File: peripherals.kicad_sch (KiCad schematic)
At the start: 61 parts, among them J8 Conn_02x25_Odd_Even, U1 MX6UL-VM

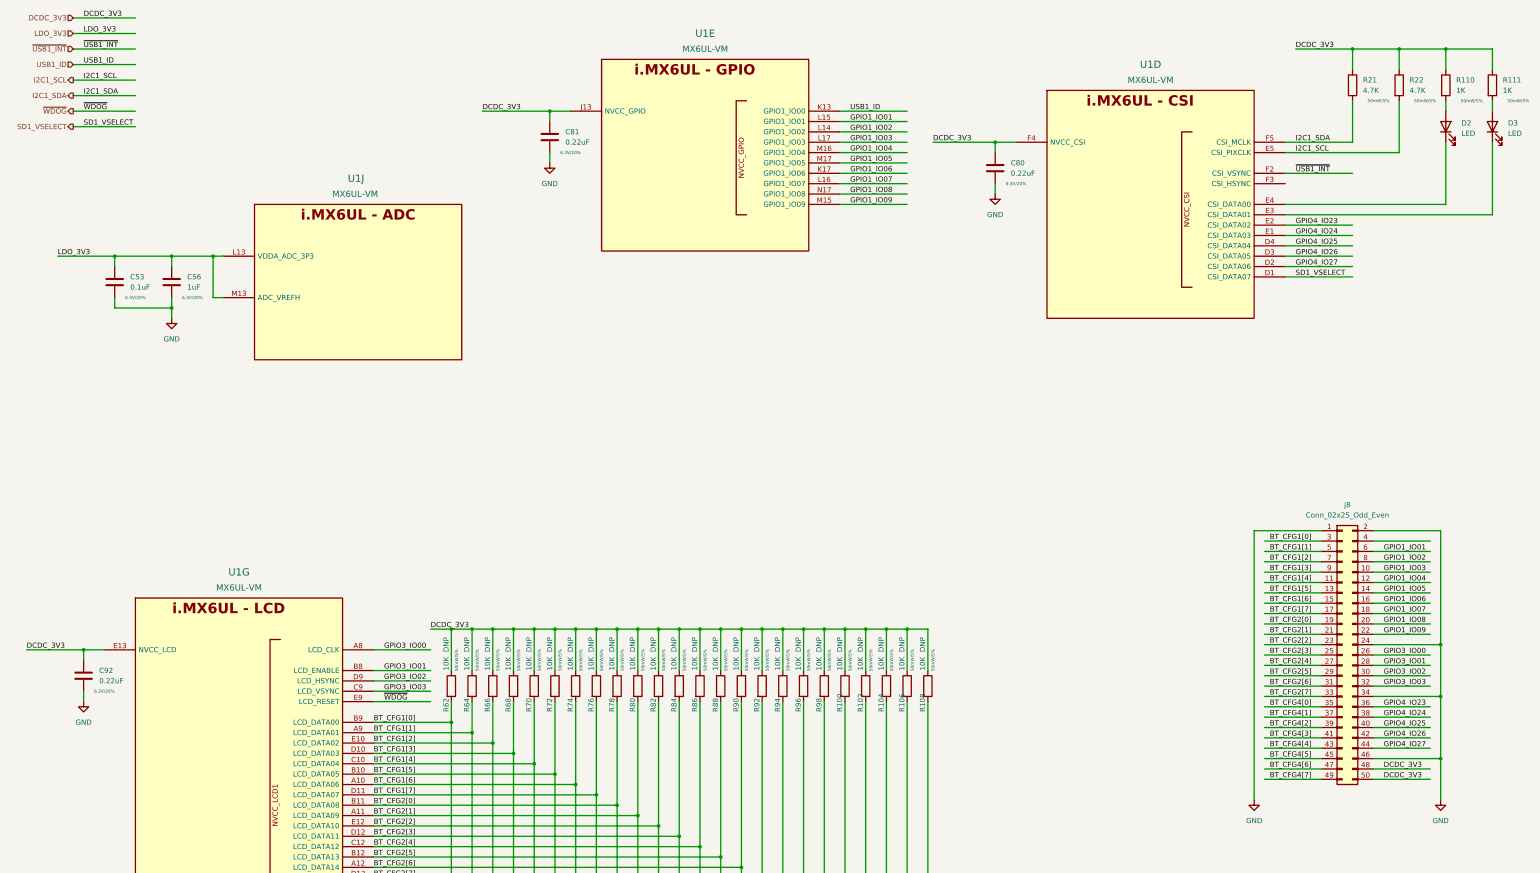
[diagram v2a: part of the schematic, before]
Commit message: most of sch done, inital component pcb placement
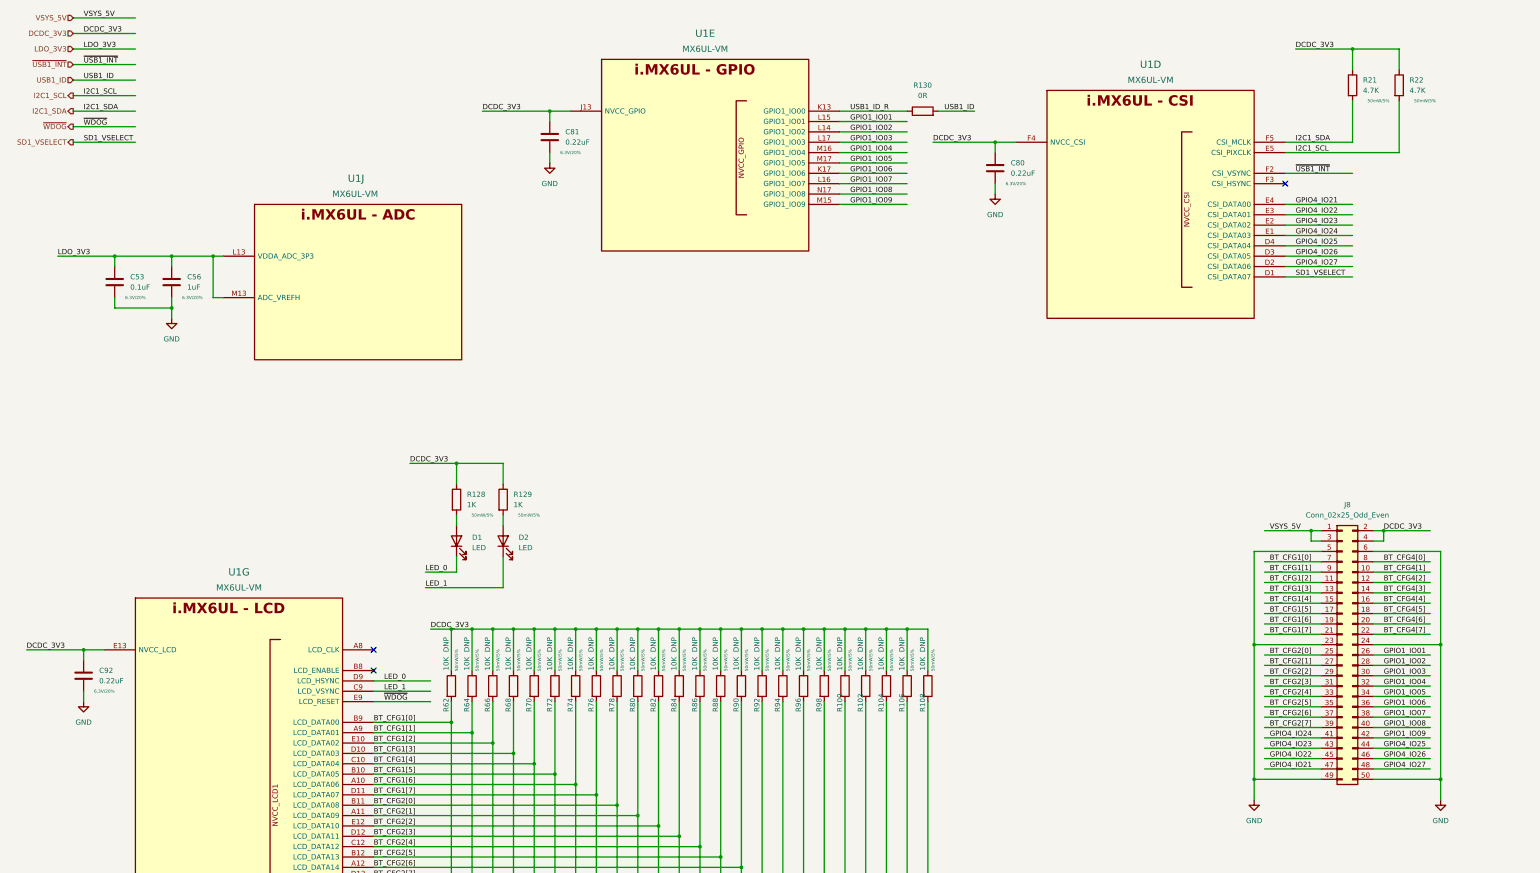
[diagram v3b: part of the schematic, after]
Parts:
- removed D3: LED, LED_SMD:LED_0603_1608Metric, symbol Device:LED
- removed R110, R111: 1K, Resistor_SMD:R_0402_1005Metric, symbol Device:R
- added D1: LED, LED_SMD:LED_0603_1608Metric, symbol Device:LED
- added R128, R129: 1K, Resistor_SMD:R_0402_1005Metric, symbol Device:R
- added R130: 0R, Resistor_SMD:R_0402_1005Metric, symbol Device:R
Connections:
- net BT_CFG1[0]: now also J8.7 (Pin_7); no longer J8.3 (Pin_3)
- net BT_CFG1[1]: now also J8.9 (Pin_9); no longer J8.5 (Pin_5)
- net BT_CFG1[2]: now also J8.11 (Pin_11); no longer J8.7 (Pin_7)
- net BT_CFG1[3]: now also J8.13 (Pin_13); no longer J8.9 (Pin_9)
- net BT_CFG1[4]: now also J8.15 (Pin_15); no longer J8.11 (Pin_11)
- net BT_CFG1[5]: now also J8.17 (Pin_17); no longer J8.13 (Pin_13)
- net BT_CFG1[6]: now also J8.19 (Pin_19); no longer J8.15 (Pin_15)
- net BT_CFG1[7]: now also J8.21 (Pin_21); no longer J8.17 (Pin_17)
- net BT_CFG2[0]: now also J8.25 (Pin_25); no longer J8.19 (Pin_19)
- net BT_CFG2[1]: now also J8.27 (Pin_27); no longer J8.21 (Pin_21)
- net BT_CFG2[2]: now also J8.29 (Pin_29); no longer J8.23 (Pin_23)
- net BT_CFG2[3]: now also J8.31 (Pin_31); no longer J8.25 (Pin_25)
- net BT_CFG2[4]: now also J8.33 (Pin_33); no longer J8.27 (Pin_27)
- net BT_CFG2[5]: now also J8.35 (Pin_35); no longer J8.29 (Pin_29)
- net BT_CFG2[6]: now also J8.37 (Pin_37); no longer J8.31 (Pin_31)
- net BT_CFG2[7]: now also J8.39 (Pin_39); no longer J8.33 (Pin_33)
- net BT_CFG4[0]: now also J8.8 (Pin_8); no longer J8.35 (Pin_35)
- net BT_CFG4[1]: now also J8.10 (Pin_10); no longer J8.37 (Pin_37)
- net BT_CFG4[2]: now also J8.12 (Pin_12); no longer J8.39 (Pin_39)
- net BT_CFG4[3]: now also J8.14 (Pin_14); no longer J8.41 (Pin_41)
- net BT_CFG4[4]: now also J8.16 (Pin_16); no longer J8.43 (Pin_43)
- net BT_CFG4[5]: now also J8.18 (Pin_18); no longer J8.45 (Pin_45)
- net BT_CFG4[6]: now also J8.20 (Pin_20); no longer J8.47 (Pin_47)
- net BT_CFG4[7]: now also J8.22 (Pin_22); no longer J8.49 (Pin_49)
- net DCDC_3V3: now also J8.2 (Pin_2), J8.4 (Pin_4), R128.1, R129.1; no longer J8.48 (Pin_48), J8.50 (Pin_50)
- net GND: now also J8.23 (Pin_23), J8.49 (Pin_49), J8.5 (Pin_5), J8.50 (Pin_50), J8.6 (Pin_6); no longer J8.1 (Pin_1), J8.2 (Pin_2), J8.34 (Pin_34), J8.46 (Pin_46)
- net GPIO1_IO01: now also J8.26 (Pin_26); no longer J8.6 (Pin_6)
- net GPIO1_IO02: now also J8.28 (Pin_28); no longer J8.8 (Pin_8)
- net GPIO1_IO03: now also J8.30 (Pin_30); no longer J8.10 (Pin_10)
- net GPIO1_IO04: now also J8.32 (Pin_32); no longer J8.12 (Pin_12)
- net GPIO1_IO05: now also J8.34 (Pin_34); no longer J8.14 (Pin_14)
- net GPIO1_IO06: now also J8.36 (Pin_36); no longer J8.16 (Pin_16)
- net GPIO1_IO07: now also J8.38 (Pin_38); no longer J8.18 (Pin_18)
- net GPIO1_IO08: now also J8.40 (Pin_40); no longer J8.20 (Pin_20)
- net GPIO1_IO09: now also J8.42 (Pin_42); no longer J8.22 (Pin_22)
- net GPIO4_IO23: now also J8.43 (Pin_43); no longer J8.36 (Pin_36)
- net GPIO4_IO24: now also J8.41 (Pin_41); no longer J8.38 (Pin_38)
- net GPIO4_IO25: now also J8.44 (Pin_44); no longer J8.40 (Pin_40)
- net GPIO4_IO26: now also J8.46 (Pin_46); no longer J8.42 (Pin_42)
- net GPIO4_IO27: now also J8.48 (Pin_48); no longer J8.44 (Pin_44)
- net USB1_ID: now also R130.2; no longer U1.K13 (GPIO1_IO00)
- net GPIO4_IO22: now reaches U1.E3 (CSI_DATA01)
- net GPIO4_IO22: now also J8.45 (Pin_45)
- net GPIO4_IO21: now reaches U1.E4 (CSI_DATA00)
- net GPIO4_IO21: now also J8.47 (Pin_47); no longer D2.1 (K)
- net at D2.2 (A): now also R129.2
- net GPIO3_IO00: no longer names the net of U1.A8 (LCD_CLK)
- net GPIO3_IO00: no longer J8.26 (Pin_26)
- net GPIO3_IO01: no longer names the net of U1.B8 (LCD_ENABLE)
- net GPIO3_IO01: no longer J8.28 (Pin_28)
- net GPIO3_IO02 renamed LED_0
- net LED_0: now also D1.1 (K); no longer J8.30 (Pin_30)
- net GPIO3_IO03 renamed LED_1
- net LED_1: now also D2.1 (K); no longer J8.32 (Pin_32)
- new net: D1.2 (A), R128.2
- new net USB1_ID_R: R130.1, U1.K13 (GPIO1_IO00)
- new net VSYS_5V: J8.1 (Pin_1), J8.3 (Pin_3)
- no-connect marks 0 -> 3

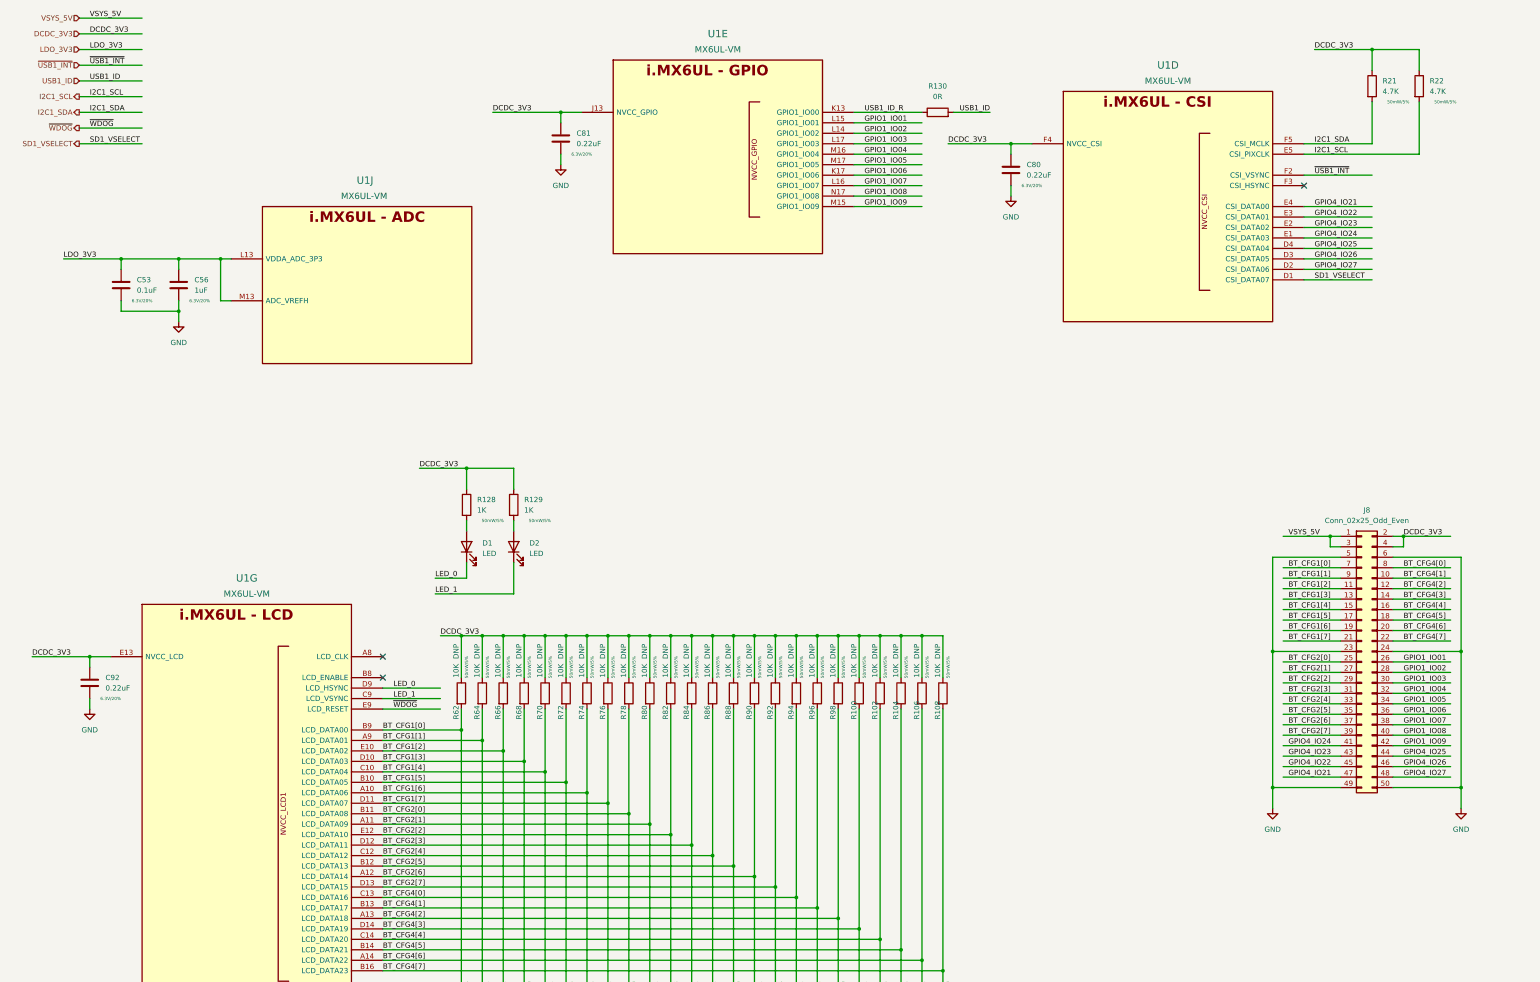
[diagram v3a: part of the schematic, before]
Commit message: lots of routing, ddr length matching done
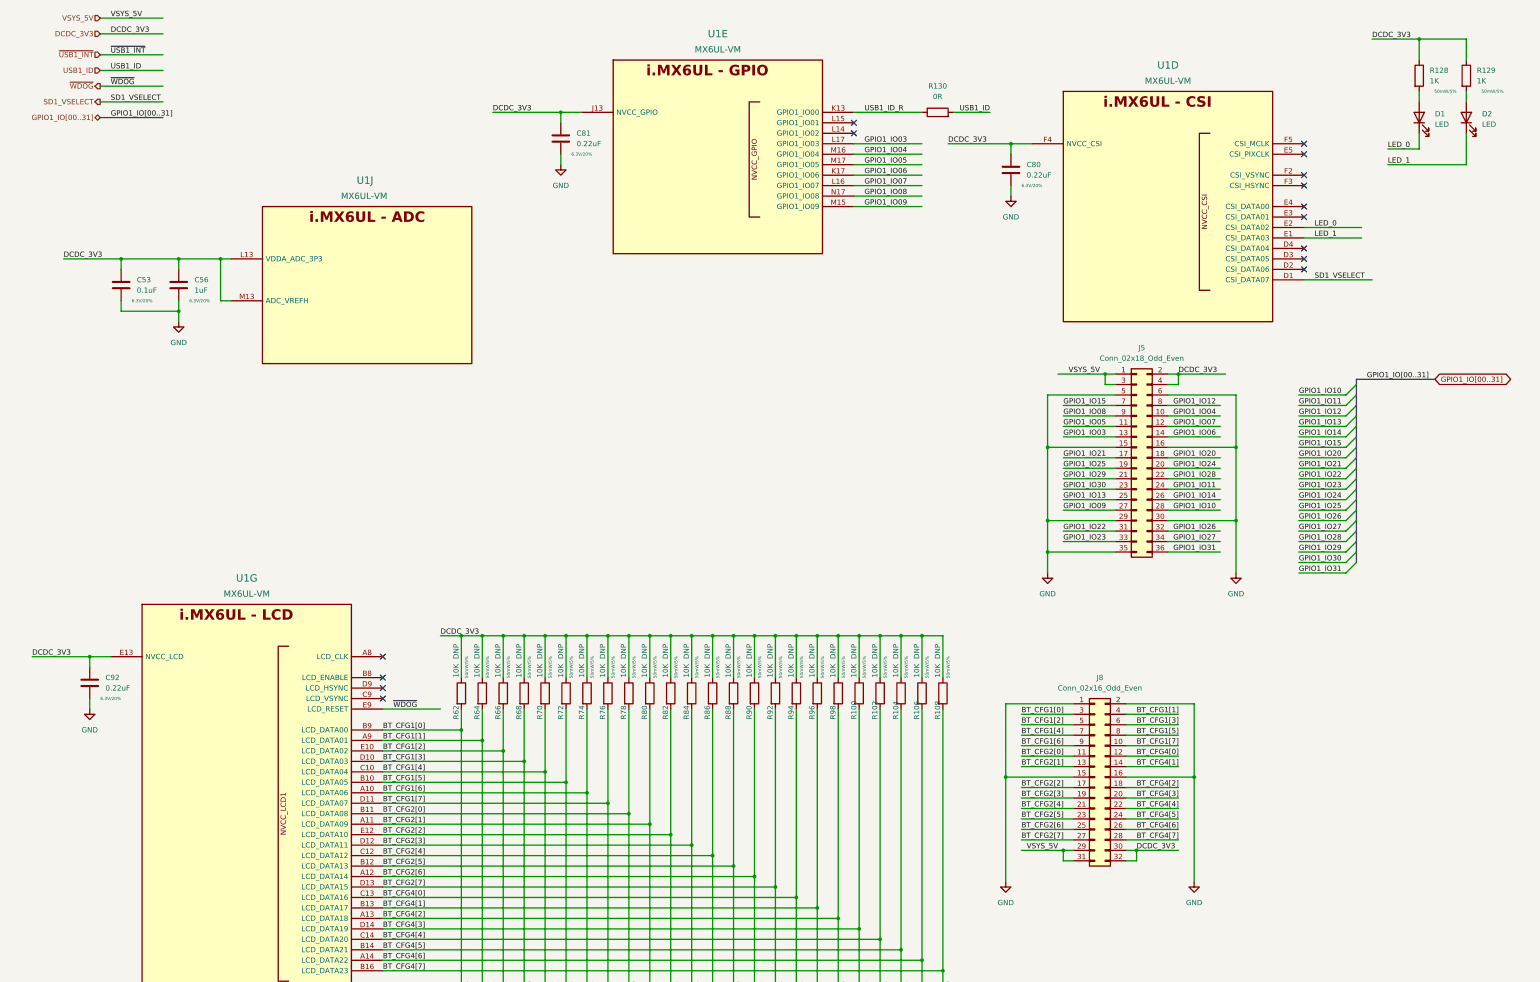
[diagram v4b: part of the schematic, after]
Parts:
- removed J8: Conn_02x25_Odd_Even, Connector_PinHeader_2.54mm:PinHeader_2x25_P2.54mm_Vertical_SMD, symbol Connector_Generic:Conn_02x25_Odd_Even
- removed R21, R22: 4.7K, Resistor_SMD:R_0402_1005Metric, symbol Device:R
- added J5: Conn_02x18_Odd_Even, Connector_PinHeader_2.54mm:PinHeader_2x18_P2.54mm_Vertical, symbol Connector_Generic:Conn_02x18_Odd_Even
- added J8: Conn_02x16_Odd_Even, Connector_PinHeader_2.54mm:PinHeader_2x16_P2.54mm_Vertical, symbol Connector_Generic:Conn_02x16_Odd_Even
- C53, C80, C81, C92: footprint Capacitor_SMD:C_0402_1005Metric -> Capacitor_SMD:C_0201_0603Metric
- U1: footprint imx6ull-sbc:SOT1534-2 -> qsbc-zero:SOT1534-2; symbol imx6ull-sbc:MX6UL-VM -> qsbc-zero:MX6UL-VM
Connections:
- net GPIO4_IO23 is gone; now on net LED_0: U1.E2 (CSI_DATA02)
- net GPIO4_IO24 is gone; now on net LED_1: U1.E1 (CSI_DATA03)
- net LDO_3V3 is gone; now on net DCDC_3V3: C53.1, C56.1, U1.L13 (VDDA_ADC_3P3), U1.M13 (ADC_VREFH)
- net BT_CFG1[0]: now also J8.3 (Pin_3)
- net BT_CFG1[1]: now also J8.4 (Pin_4)
- net BT_CFG1[2]: now also J8.5 (Pin_5)
- net BT_CFG1[3]: now also J8.6 (Pin_6)
- net BT_CFG1[4]: now also J8.7 (Pin_7)
- net BT_CFG1[5]: now also J8.8 (Pin_8)
- net BT_CFG1[6]: now also J8.9 (Pin_9)
- net BT_CFG1[7]: now also J8.10 (Pin_10)
- net BT_CFG2[0]: now also J8.11 (Pin_11)
- net BT_CFG2[1]: now also J8.13 (Pin_13)
- net BT_CFG2[2]: now also J8.17 (Pin_17)
- net BT_CFG2[3]: now also J8.19 (Pin_19)
- net BT_CFG2[4]: now also J8.21 (Pin_21)
- net BT_CFG2[5]: now also J8.23 (Pin_23)
- net BT_CFG2[6]: now also J8.25 (Pin_25)
- net BT_CFG2[7]: now also J8.27 (Pin_27)
- net BT_CFG4[0]: now also J8.12 (Pin_12)
- net BT_CFG4[1]: now also J8.14 (Pin_14)
- net BT_CFG4[2]: now also J8.18 (Pin_18)
- net BT_CFG4[3]: now also J8.20 (Pin_20)
- net BT_CFG4[4]: now also J8.22 (Pin_22)
- net BT_CFG4[5]: now also J8.24 (Pin_24)
- net BT_CFG4[6]: now also J8.26 (Pin_26)
- net BT_CFG4[7]: now also J8.28 (Pin_28)
- net DCDC_3V3: now also J5.2 (Pin_2), J5.4 (Pin_4), J8.30 (Pin_30), J8.32 (Pin_32)
- net GND: now also J5.15 (Pin_15), J5.16 (Pin_16), J5.29 (Pin_29), J5.30 (Pin_30), J5.35 (Pin_35), J5.5 (Pin_5), J5.6 (Pin_6), J8.1 (Pin_1), J8.15 (Pin_15), J8.16 (Pin_16), J8.2 (Pin_2)
- net GPIO1_IO03: now also J5.13 (Pin_13)
- net GPIO1_IO04: now also J5.10 (Pin_10)
- net GPIO1_IO05: now also J5.11 (Pin_11)
- net GPIO1_IO06: now also J5.14 (Pin_14)
- net GPIO1_IO07: now also J5.12 (Pin_12)
- net GPIO1_IO08: now also J5.9 (Pin_9)
- net GPIO1_IO09: now also J5.27 (Pin_27)
- net LED_0: no longer U1.D9 (LCD_HSYNC)
- net LED_1: no longer U1.C9 (LCD_VSYNC)
- net VSYS_5V: now also J5.1 (Pin_1), J5.3 (Pin_3), J8.29 (Pin_29), J8.31 (Pin_31)
- net ~{USB1_INT}: no longer U1.F2 (CSI_VSYNC)
- net GPIO1_IO01: no longer names the net of U1.L15 (GPIO1_IO01)
- net GPIO1_IO02: no longer names the net of U1.L14 (GPIO1_IO02)
- net GPIO4_IO21: no longer names the net of U1.E4 (CSI_DATA00)
- net GPIO4_IO22: no longer names the net of U1.E3 (CSI_DATA01)
- net GPIO4_IO25: no longer names the net of U1.D4 (CSI_DATA04)
- net GPIO4_IO26: no longer names the net of U1.D3 (CSI_DATA05)
- net GPIO4_IO27: no longer names the net of U1.D2 (CSI_DATA06)
- net I2C1_SCL: no longer names the net of U1.E5 (CSI_PIXCLK)
- net I2C1_SDA: no longer names the net of U1.F5 (CSI_MCLK)
- new net GPIO1_IO10: J5.28 (Pin_28)
- new net GPIO1_IO11: J5.24 (Pin_24)
- new net GPIO1_IO12: J5.8 (Pin_8)
- new net GPIO1_IO13: J5.25 (Pin_25)
- new net GPIO1_IO14: J5.26 (Pin_26)
- new net GPIO1_IO15: J5.7 (Pin_7)
- new net GPIO1_IO20: J5.18 (Pin_18)
- new net GPIO1_IO21: J5.17 (Pin_17)
- new net GPIO1_IO22: J5.31 (Pin_31)
- new net GPIO1_IO23: J5.33 (Pin_33)
- new net GPIO1_IO24: J5.20 (Pin_20)
- new net GPIO1_IO25: J5.19 (Pin_19)
- new net GPIO1_IO26: J5.32 (Pin_32)
- new net GPIO1_IO27: J5.34 (Pin_34)
- new net GPIO1_IO28: J5.22 (Pin_22)
- new net GPIO1_IO29: J5.21 (Pin_21)
- new net GPIO1_IO30: J5.23 (Pin_23)
- new net GPIO1_IO31: J5.36 (Pin_36)
- no-connect marks 3 -> 15
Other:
- moved on the sheet: D1, D2, R128, R129
